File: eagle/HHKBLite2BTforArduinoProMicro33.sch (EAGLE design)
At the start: 40 parts, among them CON1 45045-1445, CON2 45045-0845, IC1 4514N, IC2 4512N, IC4 HT7733A, J1 J7MM, J2 J15MM, J3 J7MM, J4 J10MM

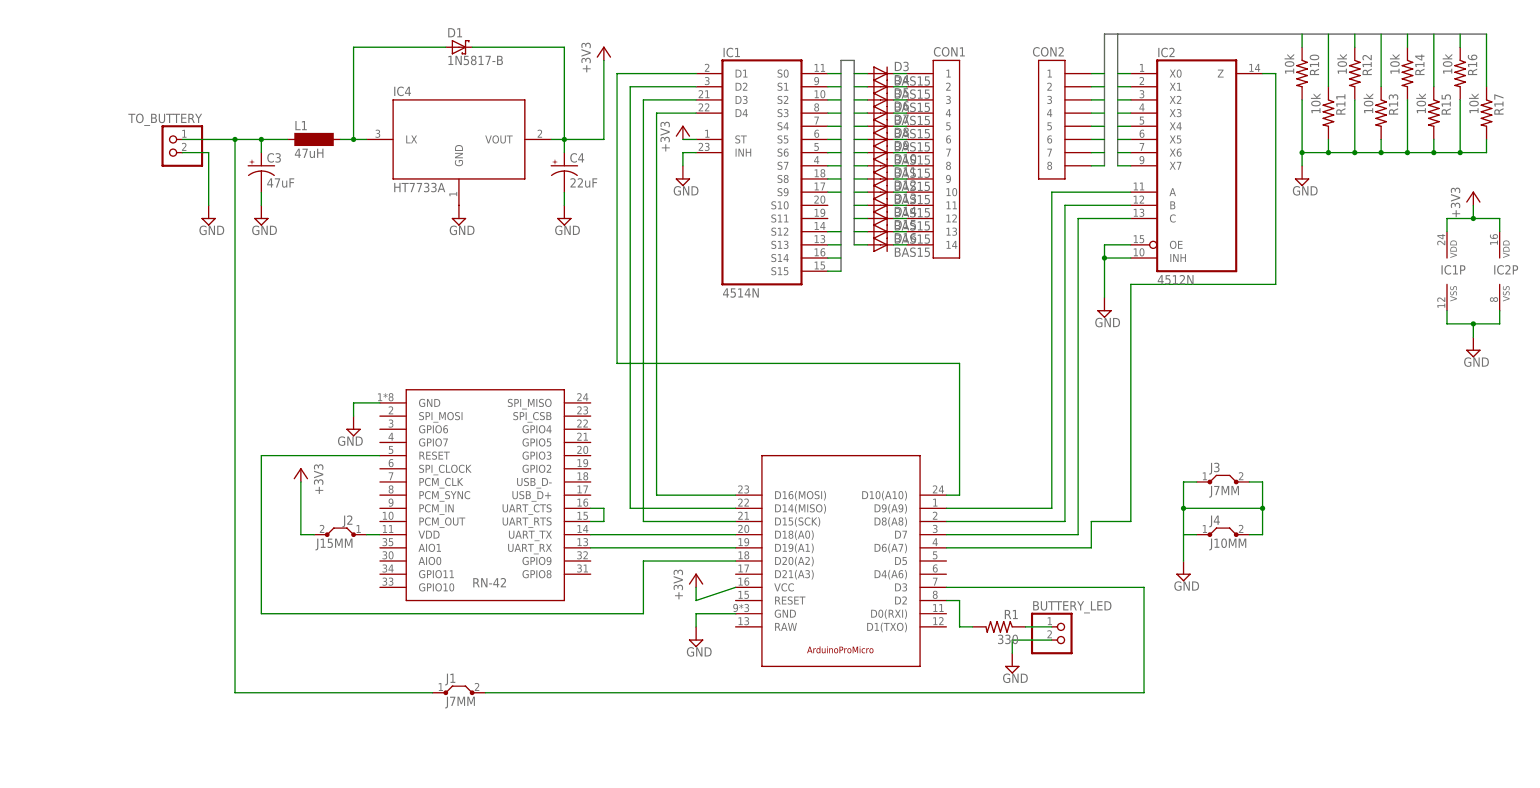
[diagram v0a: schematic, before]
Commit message: いろいろ変えた
回路図については, 電源周りとかアライメントとかを調節した.
また, パーツのサイズを, 実際に使いそうなサイズにフィットさせた.
プログラムは移動させた.
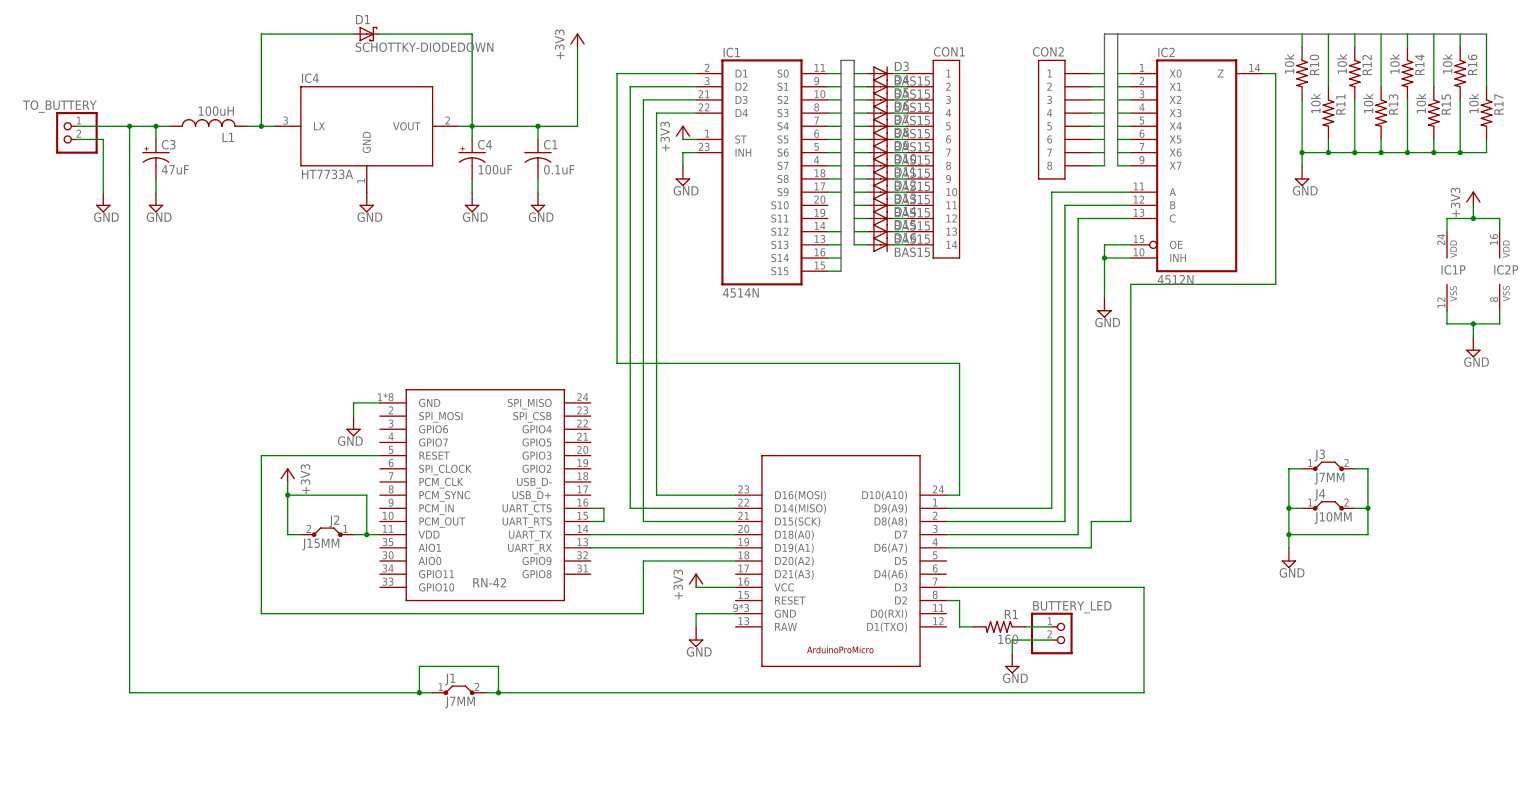
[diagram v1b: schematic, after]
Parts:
- added C1: 0.1uF, rcl:C-US050-024X044
- C3: device rcl:CPOL-USE5-10.5 -> rcl:CPOL-USE2.5-7
- C4: value 22uF -> 100uF; device rcl:CPOL-USE5-10.5 -> rcl:CPOL-USE2.5-7
- D1: value 1N5817-B -> SCHOTTKY-DIODEDOWN; device diode:1N5817-B -> MySilicon:SCHOTTKY-DIODEDOWN
- L1: value 47uH -> 100uH; device inductor-neosid:BS11 -> MyRCL:LL5-10
- R1: value 330 -> 160
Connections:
- removed net N$10: J2.1, U$1.VDD
- removed net N$8: J1.2, U$2.D3
- net +3V3: now also C1.1, J2.1, U$1.VDD
- net GND: now also C1.2
- net N$4: now also J1.2, U$2.D3
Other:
- moved on the sheet: C3, C4, D1, IC4, J2, J3, J4, TO_BUTTERY

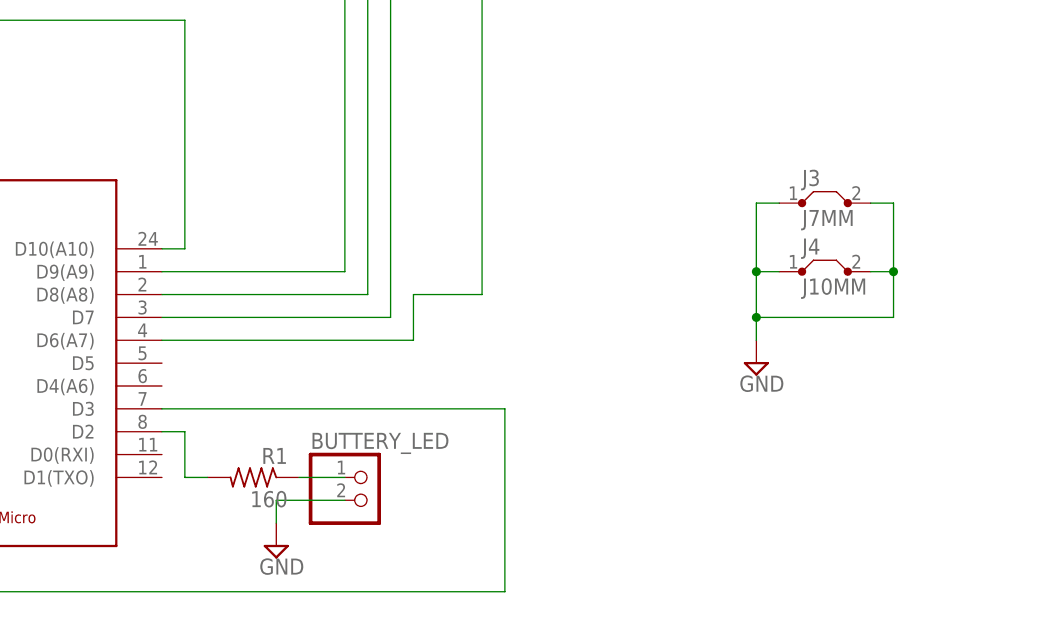
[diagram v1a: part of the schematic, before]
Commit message: ProMicro33用コードと回路図を変更
各ICとのピンの番号が整合するように調節した.
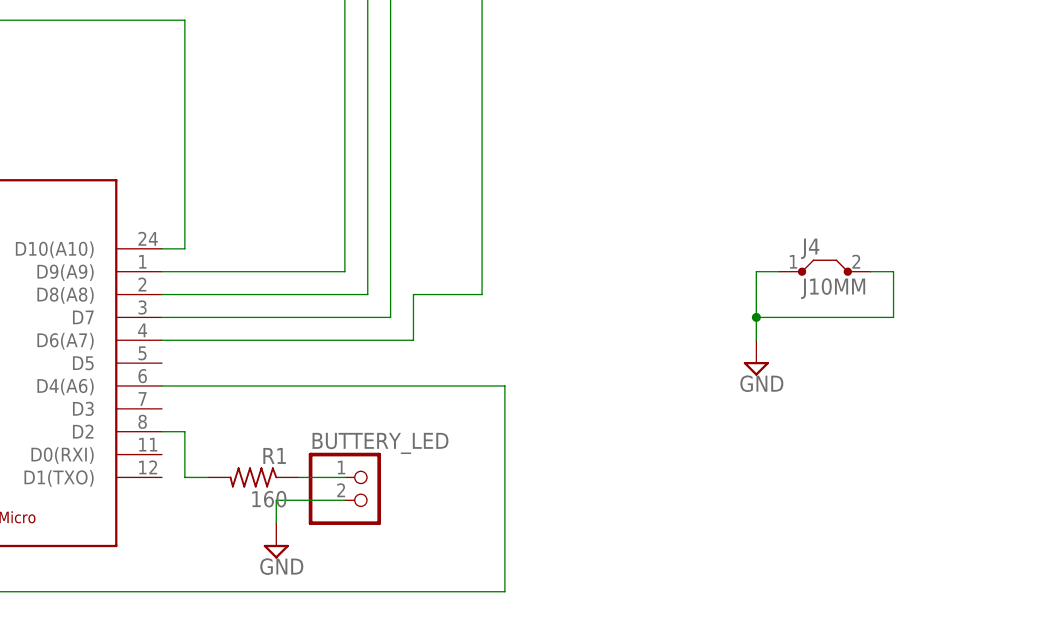
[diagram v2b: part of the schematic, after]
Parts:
- removed J3: J7MM, jumper:J7MM
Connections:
- removed net N$4: C3.+, J1.1, J1.2, L1.1, TO_BUTTERY.1, U$2.D3
- new net VCC_SRC: C3.+, J1.1, J1.2, L1.1, TO_BUTTERY.1, U$2.D4(A6)
- net GND: no longer J3.1, J3.2
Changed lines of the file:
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@@
 </class>
 <class number="1" name="Vcc" width="0.0254" drill="0">
-<clearance class="0" value="0.508"/>
+<clearance class="1" value="0.205"/>
 </class>
 <class number="2" name="VccSrc" width="0" drill="0">
-<clearance class="0" value="0.508"/>
-<clearance class="1" value="0.508"/>
 <clearance class="2" value="0.508"/>
 </class>
 <class number="3" name="GND" width="0" drill="0">
-<clearance class="0" value="0.3048"/>
 <clearance class="1" value="0.508"/>
 <clearance class="2" value="0.508"/>
+<clearance class="3" value="0.205"/>
 </class>
 </classes>
@@
 <part name="SUPPLY8" library="supply2" deviceset="GND" device=""/>
 <part name="SUPPLY9" library="supply2" deviceset="GND" device=""/>
-<part name="J3" library="jumper" deviceset="J" device="7MM"/>
 </parts>
 <sheets>
@@
 <instance part="SUPPLY8" gate="GND" x="71.12" y="106.68"/>
 <instance part="SUPPLY9" gate="GND" x="215.9" y="38.1"/>
-<instance part="J3" gate="1" x="223.52" y="55.88"/>
 </instances>
 <busses>
@@
 <pinref part="SUPPLY9" gate="GND" pin="GND"/>
 <wire x1="215.9" y1="40.64" x2="215.9" y2="43.18" width="0.1524" layer="91"/>
-<pinref part="J3" gate="1" pin="1"/>
 <wire x1="215.9" y1="43.18" x2="215.9" y2="48.26" width="0.1524" layer="91"/>
-<wire x1="215.9" y1="48.26" x2="215.9" y2="55.88" width="0.1524" layer="91"/>
-<wire x1="215.9" y1="55.88" x2="218.44" y2="55.88" width="0.1524" layer="91"/>
 <pinref part="J4" gate="1" pin="1"/>
 <wire x1="218.44" y1="48.26" x2="215.9" y2="48.26" width="0.1524" layer="91"/>
 <wire x1="215.9" y1="43.18" x2="231.14" y2="43.18" width="0.1524" layer="91"/>
 <wire x1="231.14" y1="43.18" x2="231.14" y2="48.26" width="0.1524" layer="91"/>
-<pinref part="J3" gate="1" pin="2"/>
-<wire x1="231.14" y1="48.26" x2="231.14" y2="55.88" width="0.1524" layer="91"/>
-<wire x1="231.14" y1="55.88" x2="228.6" y2="55.88" width="0.1524" layer="91"/>
 <pinref part="J4" gate="1" pin="2"/>
 <wire x1="228.6" y1="48.26" x2="231.14" y2="48.26" width="0.1524" layer="91"/>
-<junction x="215.9" y="48.26"/>
-<junction x="231.14" y="48.26"/>
 <junction x="215.9" y="43.18"/>
 </segment>
@@
 </segment>
 </net>
-<net name="N$4" class="2">
+<net name="VCC_SRC" class="2">
 <segment>
 <pinref part="C3" gate="G$1" pin="+"/>
@@
 <junction x="-2.54" y="121.92"/>
 <wire x1="48.26" y1="12.7" x2="48.26" y2="17.78" width="0.1524" layer="91"/>
-<pinref part="U$2" gate="G$1" pin="D3"/>
-<wire x1="187.96" y1="12.7" x2="187.96" y2="33.02" width="0.1524" layer="91"/>
-<wire x1="187.96" y1="33.02" x2="149.86" y2="33.02" width="0.1524" layer="91"/>
+<wire x1="187.96" y1="12.7" x2="187.96" y2="35.56" width="0.1524" layer="91"/>
 <wire x1="187.96" y1="12.7" x2="63.5" y2="12.7" width="0.1524" layer="91"/>
 <pinref part="J1" gate="1" pin="2"/>
@@
 <junction x="48.26" y="12.7"/>
 <junction x="63.5" y="12.7"/>
-</segment>
-</net>
+<pinref part="U$2" gate="G$1" pin="D4(A6)"/>
+<wire x1="149.86" y1="35.56" x2="187.96" y2="35.56" width="0.1524" layer="91"/>
+</segment>
+</net>

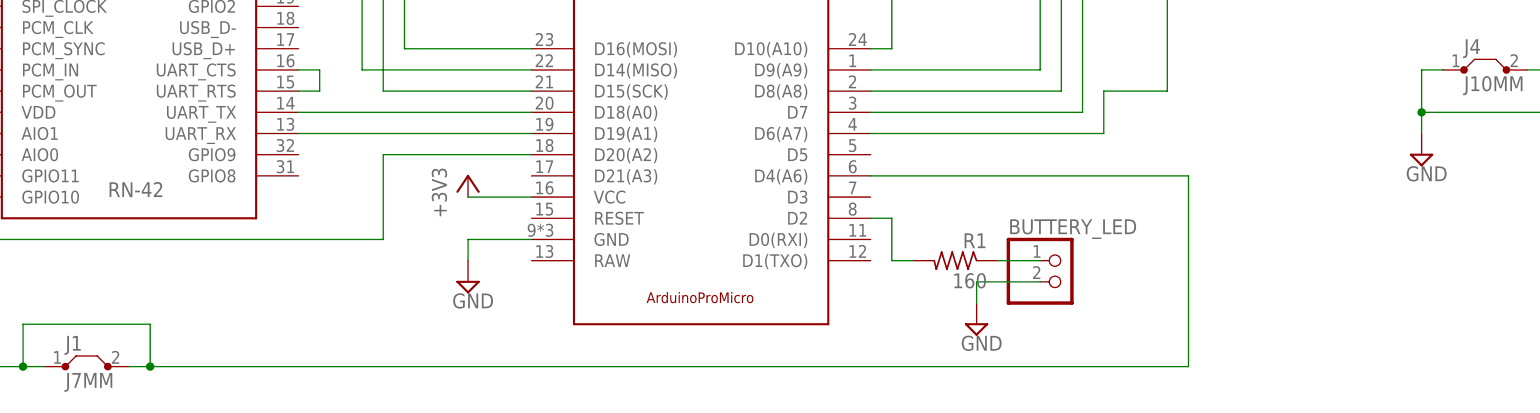
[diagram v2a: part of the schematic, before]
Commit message: 入力ピンをINPUTからINPUT_PULLUPに変更
内部プルアップ抵抗を使うように書き換えた.
それに伴い, 該当箇所の真理値を逆転させた.
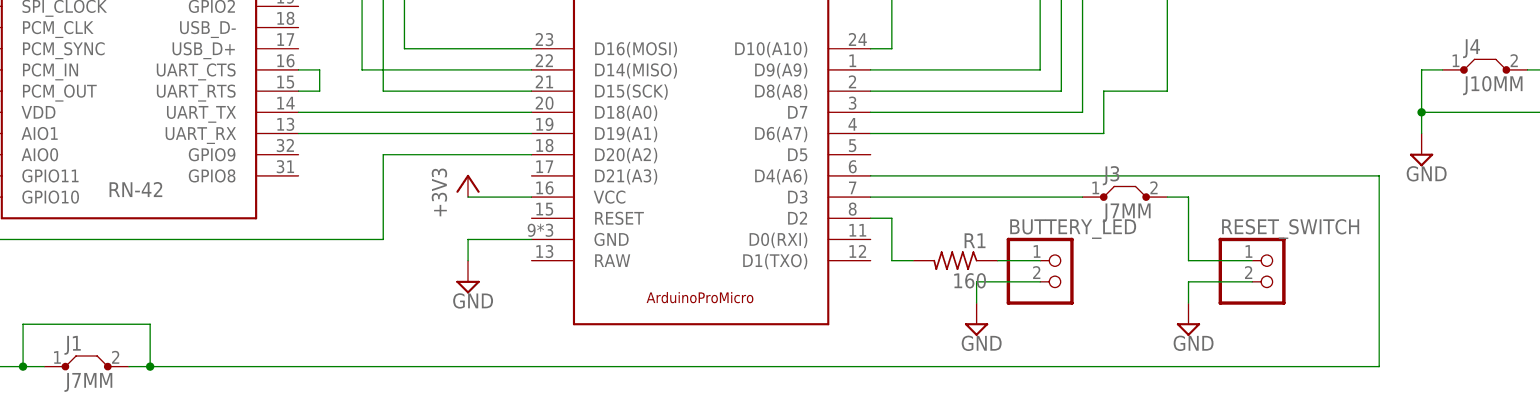
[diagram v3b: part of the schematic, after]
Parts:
- added J3: J7MM, jumper:J7MM
- added RESET_SWITCH: (no value), pinhead:PINHD-1X2
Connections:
- new net N$4: J3.2, RESET_SWITCH.1
- new net N$8: J3.1, U$2.D3
- net GND: now also RESET_SWITCH.2
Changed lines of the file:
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@@
 <part name="SUPPLY8" library="supply2" deviceset="GND" device=""/>
 <part name="SUPPLY9" library="supply2" deviceset="GND" device=""/>
+<part name="RESET_SWITCH" library="pinhead" deviceset="PINHD-1X2" device=""/>
+<part name="SUPPLY3" library="supply2" deviceset="GND" device=""/>
+<part name="J3" library="jumper" deviceset="J" device="7MM"/>
 </parts>
 <sheets>
@@
 <instance part="SUPPLY8" gate="GND" x="71.12" y="106.68"/>
 <instance part="SUPPLY9" gate="GND" x="215.9" y="38.1"/>
+<instance part="RESET_SWITCH" gate="G$1" x="198.12" y="22.86"/>
+<instance part="SUPPLY3" gate="GND" x="187.96" y="17.78"/>
+<instance part="J3" gate="1" x="180.34" y="33.02"/>
 </instances>
 <busses>
@@
 <junction x="215.9" y="43.18"/>
 </segment>
+<segment>
+<pinref part="RESET_SWITCH" gate="G$1" pin="2"/>
+<wire x1="195.58" y1="22.86" x2="187.96" y2="22.86" width="0.1524" layer="91"/>
+<wire x1="187.96" y1="22.86" x2="187.96" y2="20.32" width="0.1524" layer="91"/>
+<pinref part="SUPPLY3" gate="GND" pin="GND"/>
+</segment>
 </net>
 <net name="N$3" class="2">
@@
 <junction x="-2.54" y="121.92"/>
 <wire x1="48.26" y1="12.7" x2="48.26" y2="17.78" width="0.1524" layer="91"/>
-<wire x1="187.96" y1="12.7" x2="187.96" y2="35.56" width="0.1524" layer="91"/>
-<wire x1="187.96" y1="12.7" x2="63.5" y2="12.7" width="0.1524" layer="91"/>
+<wire x1="210.82" y1="12.7" x2="210.82" y2="35.56" width="0.1524" layer="91"/>
+<wire x1="210.82" y1="12.7" x2="63.5" y2="12.7" width="0.1524" layer="91"/>
 <pinref part="J1" gate="1" pin="2"/>
 <wire x1="63.5" y1="12.7" x2="60.96" y2="12.7" width="0.1524" layer="91"/>
@@
 <junction x="63.5" y="12.7"/>
 <pinref part="U$2" gate="G$1" pin="D4(A6)"/>
-<wire x1="149.86" y1="35.56" x2="187.96" y2="35.56" width="0.1524" layer="91"/>
+<wire x1="149.86" y1="35.56" x2="210.82" y2="35.56" width="0.1524" layer="91"/>
 </segment>
 </net>
@@
 </segment>
 </net>
+<net name="N$4" class="0">
+<segment>
+<wire x1="187.96" y1="33.02" x2="187.96" y2="25.4" width="0.1524" layer="91"/>
+<pinref part="RESET_SWITCH" gate="G$1" pin="1"/>
+<wire x1="187.96" y1="25.4" x2="195.58" y2="25.4" width="0.1524" layer="91"/>
+<pinref part="J3" gate="1" pin="2"/>
+<wire x1="185.42" y1="33.02" x2="187.96" y2="33.02" width="0.1524" layer="91"/>
+</segment>
+</net>
+<net name="N$8" class="0">
+<segment>
+<pinref part="U$2" gate="G$1" pin="D3"/>
+<pinref part="J3" gate="1" pin="1"/>
+<wire x1="149.86" y1="33.02" x2="175.26" y2="33.02" width="0.1524" layer="91"/>
+</segment>
+</net>
